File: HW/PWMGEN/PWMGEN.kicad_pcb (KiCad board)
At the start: 2 copper layers, 97.8 x 99.1 mm, 28 parts, among them Q1 MMBT3904, U2 MCP1825ST-3302E/DB, U3 uA78M05C, U4 STM32L011D4Px, U5 LM4132AMF-3.3

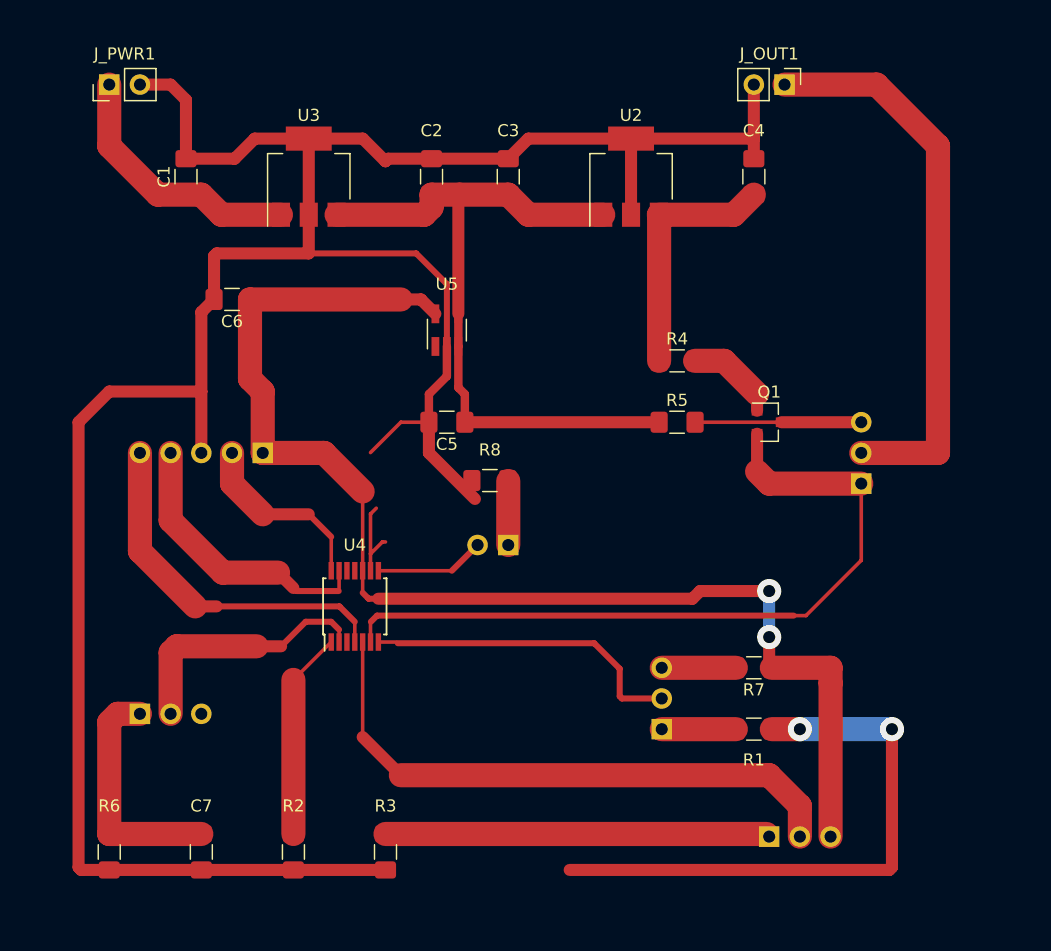
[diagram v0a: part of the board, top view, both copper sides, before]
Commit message: updated layout
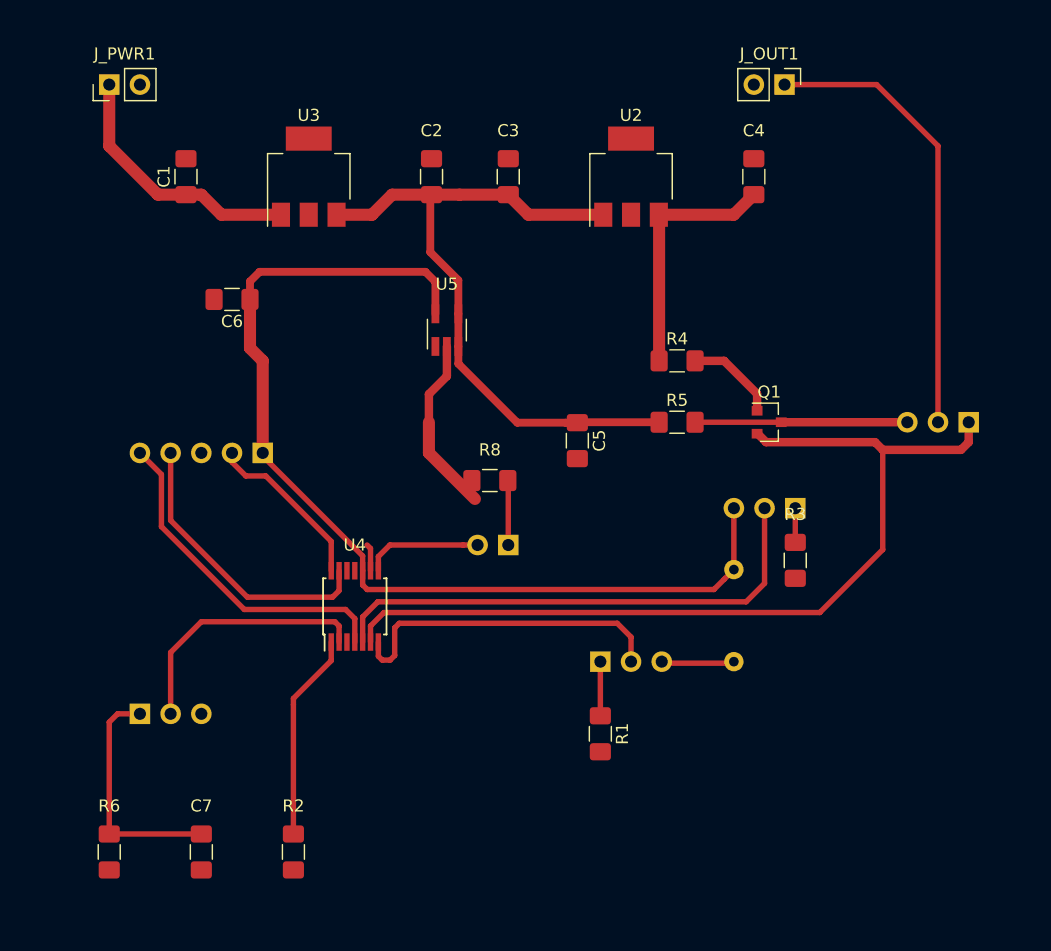
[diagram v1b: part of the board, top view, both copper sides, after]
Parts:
- R7: footprint Resistor_SMD:R_1206_3216Metric_Pad1.42x1.75mm_HandSolder -> Resistor_THT:R_Axial_DIN0207_L6.3mm_D2.5mm_P7.62mm_Horizontal; moved to B.Cu
- moved R3 41.6 mm to (148.2, 105.4)
- moved J_RV_PWM1 27.3 mm to (148.2, 101.1), turned to 90 degrees
- moved R1 12.7 mm to (132.1, 119.8), turned to 270 degrees
- moved C5 10.9 mm to (130.2, 95.5), turned to 270 degrees
- moved LVLSW1 10.2 mm to (162.6, 94.0), turned to 90 degrees
- moved R7 8.29 mm to (143.1, 106.2), turned to 270 degrees
- moved J_RV_FREQ1 7.55 mm to (132.1, 113.8), turned to 270 degrees
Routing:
- net GNDS: track 272.0 -> 17.1 mm, vias 2 -> 0
- net Net-(J_RV_PWM1-Pad1): track 31.8 -> 2.83 mm
- net +3.3VA: track 106.3 -> 84.3 mm, vias 2 -> 0
- net /3V3SIG: track 62.9 -> 74.6 mm
- net Net-(J_OUT1-Pad1): track 46.6 -> 37.7 mm
- net /PWMADJUST: track 48.9 -> 42.7 mm
- net /5VSIG: track 13.8 -> 17.6 mm
- net +5V: track 59.2 -> 57.1 mm
- net /SWRST: track 30.0 -> 27.9 mm
- net Net-(J_RV_FREQ1-Pad1): track 6.13 -> 4.48 mm
- net Net-(J_ACTIVE1-Pad1): track 6.62 -> 5.35 mm
- net /SWCLK: track 15.4 -> 14.1 mm
- net /FREQADJUST: track 26.6 -> 27.3 mm
- net /ACTIVE: track 9.09 -> 9.78 mm

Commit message: updated layout
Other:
- board size 97.8 x 99.1 mm -> 97.8 x 74.9 mm
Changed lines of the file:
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@@
     (thickness 1.6)
     (drawings 4)
-    (tracks 125)
+    (tracks 123)
     (zones 0)
     (modules 28)
@@
   )
   (setup
-    (last_trace_width 0.65)
+    (last_trace_width 0.25)
     (user_trace_width 0.3)
     (user_trace_width 0.45)
@@
     (add_net "Net-(Q1-Pad1)")
     (add_net "Net-(R2-Pad1)")
-    (add_net "Net-(U4-Pad11)")
-    (add_net "Net-(U4-Pad12)")
-    (add_net "Net-(U4-Pad3)")
-    (add_net "Net-(U5-Pad1)")
   )
   (module Resistor_SMD:R_1206_3216Metric_Pad1.42x1.75mm_HandSolder (layer F.Cu)
@@
     )
   )
-  (gr_line (start 76.2 149.86) (end 76.2 50.8) (layer Edge.Cuts) (width 0.05))
-  (gr_line (start 173.99 149.86) (end 76.2 149.86) (layer Edge.Cuts) (width 0.05))
-  (gr_line (start 173.99 50.8) (end 173.99 149.86) (layer Edge.Cuts) (width 0.05))
-  (gr_line (start 76.2 50.8) (end 173.99 50.8) (layer Edge.Cuts) (width 0.05))
+  (gr_line (start 76.2 134.62) (end 76.2 59.69) (layer Edge.Cuts) (width 0.05))
+  (gr_line (start 173.99 134.62) (end 76.2 134.62) (layer Edge.Cuts) (width 0.05))
+  (gr_line (start 173.99 59.69) (end 173.99 134.62) (layer Edge.Cuts) (width 0.05))
+  (gr_line (start 76.2 59.69) (end 173.99 59.69) (layer Edge.Cuts) (width 0.05))
   (segment (start 119.38 87.71) (end 119.38 90.17) (width 0.7) (layer F.Cu) (net 1))
   (segment (start 117.8925 91.6575) (end 117.8925 93.98) (width 0.7) (layer F.Cu) (net 1))
@@
   (segment (start 120.33 85.01) (end 120.33 87.71) (width 0.65) (layer F.Cu) (net 3))
   (segment (start 118.11 75.1475) (end 120.4325 75.1475) (width 1) (layer F.Cu) (net 3))
-  (segment (start 136.9425 93.98) (end 130.175 93.98) (width 0.65) (layer F.Cu) (net 3))
+  (segment (start 136.9425 93.98) (end 130.175 93.98) (width 1) (layer F.Cu) (net 3))
   (segment (start 118.008 75.2495) (end 118.11 75.1475) (width 0.65) (layer F.Cu) (net 3))
   (segment (start 118.008 79.908) (end 118.008 75.2495) (width 0.65) (layer F.Cu) (net 3))
@@
   (segment (start 104.14 88.9) (end 103.0875 87.8475) (width 1) (layer F.Cu) (net 5))
   (segment (start 104.14 96.52) (end 104.14 88.9) (width 1) (layer F.Cu) (net 5))
-  (segment (start 143.129 106.172) (end 143.129 101.092) (width 0.45) (layer F.Cu) (net 5))
+  (segment (start 143.129 106.172) (end 143.129 101.092) (width 1) (layer F.Cu) (net 5))
   (segment (start 112.41 105.044) (end 104.14 96.774) (width 0.45) (layer F.Cu) (net 5))
   (segment (start 104.14 96.774) (end 104.14 96.52) (width 0.45) (layer F.Cu) (net 5))
@@
   (segment (start 147.05 93.98) (end 139.9175 93.98) (width 0.45) (layer F.Cu) (net 10))
   (segment (start 147.05 93.98) (end 157.48 93.98) (width 0.7) (layer F.Cu) (net 10))
+  (segment (start 155.448 104.521) (end 155.448 96.647) (width 0.45) (layer F.Cu) (net 11))
   (segment (start 150.241 109.728) (end 155.448 104.521) (width 0.45) (layer F.Cu) (net 11))
+  (segment (start 113.06 110.841) (end 114.173 109.728) (width 0.45) (layer F.Cu) (net 11))
   (segment (start 114.173 109.728) (end 150.241 109.728) (width 0.45) (layer F.Cu) (net 11))
-  (segment (start 113.06 110.841) (end 114.173 109.728) (width 0.45) (layer F.Cu) (net 11))
-  (segment (start 155.448 104.521) (end 155.448 96.266) (width 0.45) (layer F.Cu) (net 11))
   (segment (start 113.06 112.17) (end 113.06 110.841) (width 0.45) (layer F.Cu) (net 11))
-  (segment (start 145.095 94.93) (end 145.05 94.93) (width 0.7) (layer F.Cu) (net 11))
-  (segment (start 162.56 95.631) (end 161.925 96.266) (width 0.7) (layer F.Cu) (net 11))
-  (segment (start 162.56 93.98) (end 162.56 95.631) (width 0.7) (layer F.Cu) (net 11))
-  (segment (start 154.813 95.631) (end 155.448 96.266) (width 0.7) (layer F.Cu) (net 11))
-  (segment (start 145.796 95.631) (end 154.813 95.631) (width 0.7) (layer F.Cu) (net 11))
-  (segment (start 145.796 95.631) (end 145.095 94.93) (width 0.7) (layer F.Cu) (net 11))
-  (segment (start 155.448 96.266) (end 161.925 96.266) (width 0.7) (layer F.Cu) (net 11))
+  (segment (start 162.56 95.631) (end 162.56 93.98) (width 0.7) (layer F.Cu) (net 11))
+  (segment (start 161.671 96.52) (end 162.56 95.631) (width 0.7) (layer F.Cu) (net 11))
+  (segment (start 146.05 96.52) (end 161.671 96.52) (width 0.7) (layer F.Cu) (net 11))
+  (segment (start 145.05 95.52) (end 146.05 96.52) (width 0.7) (layer F.Cu) (net 11))
+  (segment (start 145.05 94.93) (end 145.05 95.52) (width 0.7) (layer F.Cu) (net 11))
   (segment (start 145.05 91.63) (end 142.32 88.9) (width 0.7) (layer F.Cu) (net 12))
   (segment (start 145.05 93.03) (end 145.05 91.63) (width 0.7) (layer F.Cu) (net 12))
@@
   (segment (start 96.52 113.03) (end 99.06 110.49) (width 0.45) (layer F.Cu) (net 16))
   (segment (start 96.52 118.11) (end 96.52 113.03) (width 0.45) (layer F.Cu) (net 16))
-  (segment (start 124.46 104.14) (end 124.46 98.8425) (width 0.45) (layer F.Cu) (net 17))
+  (segment (start 124.46 104.14) (end 124.46 98.8425) (width 1) (layer F.Cu) (net 17))
   (segment (start 124.46 98.8425) (end 124.4235 98.806) (width 1) (layer F.Cu) (net 17))
-  (segment (start 154.94 66.04) (end 147.32 66.04) (width 0.45) (layer F.Cu) (net 18))
-  (segment (start 160.02 71.12) (end 154.94 66.04) (width 0.45) (layer F.Cu) (net 18))
-  (segment (start 160.02 93.98) (end 160.02 71.12) (width 0.45) (layer F.Cu) (net 18))
+  (segment (start 154.94 66.04) (end 147.32 66.04) (width 1) (layer F.Cu) (net 18))
+  (segment (start 160.02 71.12) (end 154.94 66.04) (width 1) (layer F.Cu) (net 18))
+  (segment (start 160.02 93.98) (end 160.02 71.12) (width 1) (layer F.Cu) (net 18))
   (segment (start 143.002 113.919) (end 143.129 113.792) (width 0.45) (layer F.Cu) (net 19))
-  (segment (start 137.287 113.919) (end 143.002 113.919) (width 0.45) (layer F.Cu) (net 19))
+  (segment (start 137.287 113.919) (end 143.002 113.919) (width 1) (layer F.Cu) (net 19))
   (segment (start 137.16 113.792) (end 137.287 113.919) (width 0.45) (layer F.Cu) (net 19))
-  (segment (start 132.08 113.792) (end 132.08 118.2735) (width 0.45) (layer F.Cu) (net 20))
-  (segment (start 148.209 101.092) (end 148.209 103.9225) (width 0.45) (layer F.Cu) (net 21))
-  (segment (start 91.44 128.0525) (end 99.06 128.0525) (width 0.45) (layer F.Cu) (net 22))
-  (segment (start 92.13 118.11) (end 93.98 118.11) (width 0.45) (layer F.Cu) (net 22))
-  (segment (start 91.44 118.8) (end 92.13 118.11) (width 0.45) (layer F.Cu) (net 22))
-  (segment (start 91.44 128.0525) (end 91.44 118.8) (width 0.45) (layer F.Cu) (net 22))
+  (segment (start 132.08 113.792) (end 132.08 118.2735) (width 1) (layer F.Cu) (net 20))
+  (segment (start 148.209 101.092) (end 148.209 103.9225) (width 1) (layer F.Cu) (net 21))
+  (segment (start 91.44 128.0525) (end 99.06 128.0525) (width 1) (layer F.Cu) (net 22))
+  (segment (start 92.13 118.11) (end 93.98 118.11) (width 1) (layer F.Cu) (net 22))
+  (segment (start 91.44 118.8) (end 92.13 118.11) (width 1) (layer F.Cu) (net 22))
+  (segment (start 91.44 128.0525) (end 91.44 118.8) (width 1) (layer F.Cu) (net 22))
   (zone (net 1) (net_name GNDS) (layer F.Cu) (hatch edge 0.508)
     (connect_pads yes (clearance 0.508))
@@
     (polygon
       (pts
-        (xy 76.2 149.86) (xy 173.99 149.86) (xy 173.99 50.8) (xy 76.2 50.8)
+        (xy 76.2 134.62) (xy 173.99 134.62) (xy 173.99 59.69) (xy 76.2 59.69)
       )
     )

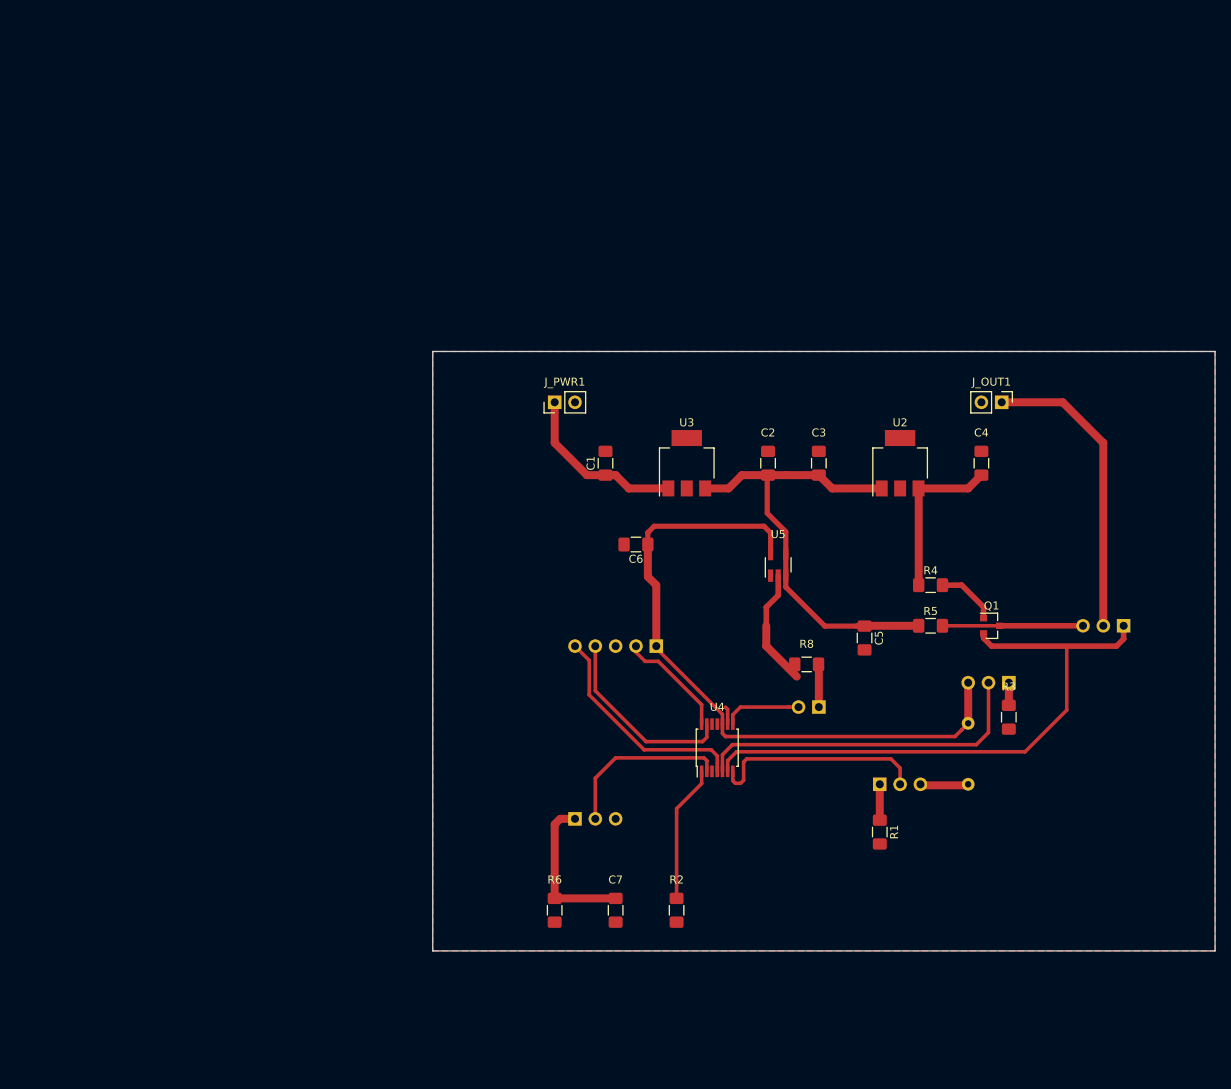
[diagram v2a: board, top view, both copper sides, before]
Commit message: updated MCU, layout, sw
- Changed from STM32L011D4 to STM32F051K8
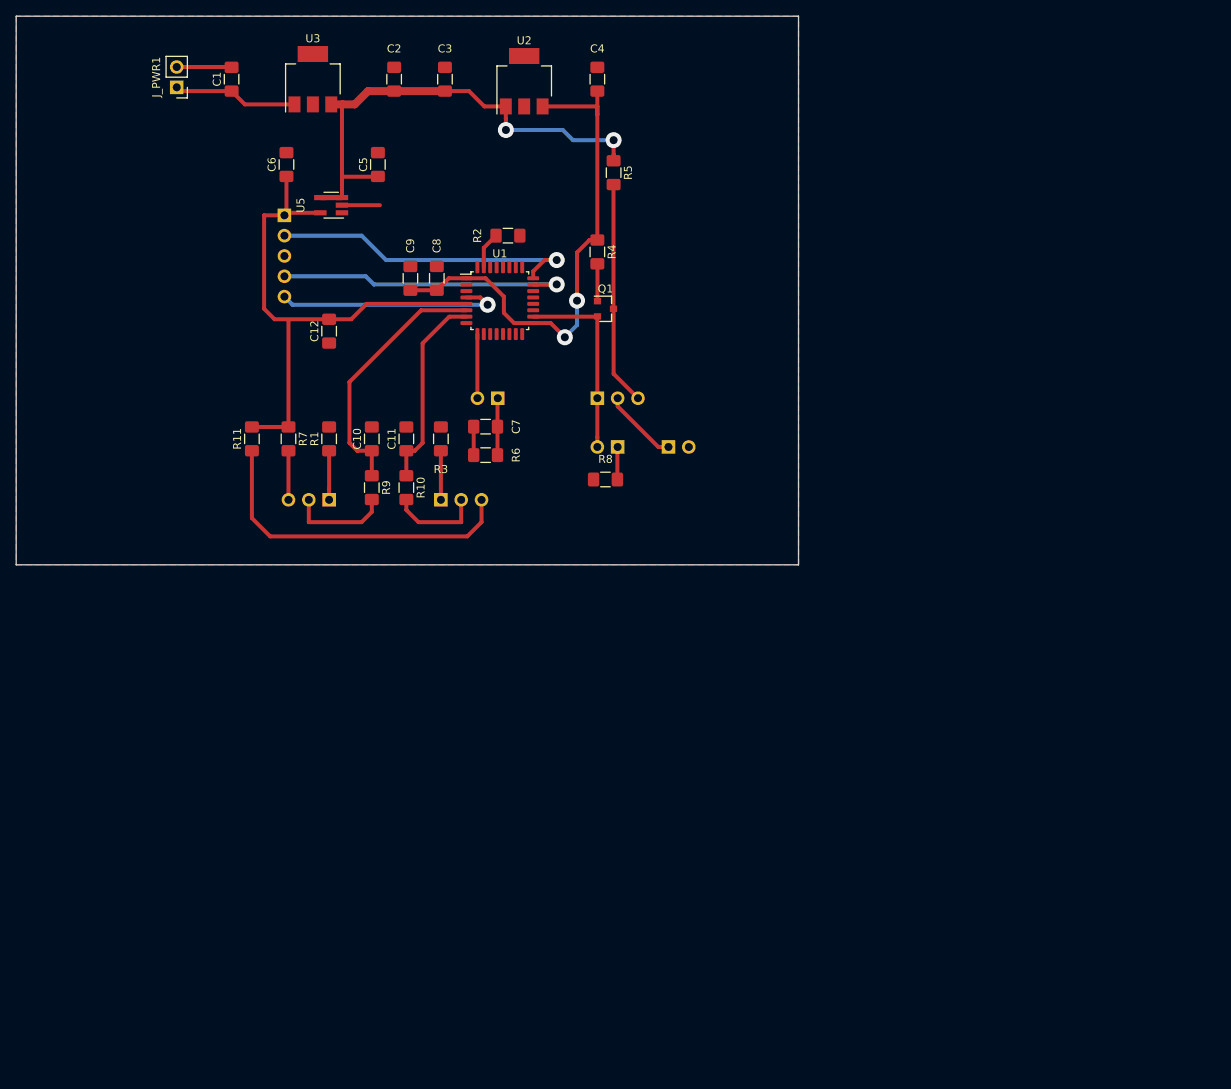
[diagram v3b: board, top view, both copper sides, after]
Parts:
- removed U4: STM32L011D4Px, Package_SO:TSSOP-14_4.4x5mm_P0.65mm
- added C10: 100n, Capacitor_SMD:C_1206_3216Metric_Pad1.42x1.75mm_HandSolder, F.Cu at (68.6, 70.6)
- added C11: 100n, Capacitor_SMD:C_1206_3216Metric_Pad1.42x1.75mm_HandSolder, F.Cu at (72.9, 70.6)
- added C12: 100n, Capacitor_SMD:C_1206_3216Metric_Pad1.42x1.75mm_HandSolder, F.Cu at (63.2, 57.1)
- added C8: 100n, Capacitor_SMD:C_1206_3216Metric_Pad1.42x1.75mm_HandSolder, F.Cu at (76.7, 50.5)
- added C9: 10uF, Capacitor_SMD:C_1206_3216Metric_Pad1.42x1.75mm_HandSolder, F.Cu at (73.4, 50.5)
- added R10: 100R, Resistor_SMD:R_1206_3216Metric_Pad1.42x1.75mm_HandSolder, F.Cu at (72.9, 76.7)
- added R11: 0R, Resistor_SMD:R_1206_3216Metric_Pad1.42x1.75mm_HandSolder, F.Cu at (53.6, 70.6)
- added R9: 100R, Resistor_SMD:R_1206_3216Metric_Pad1.42x1.75mm_HandSolder, F.Cu at (68.6, 76.7)
- added U1: STM32F051K8Tx, Package_QFP:LQFP-32_7x7mm_P0.8mm, F.Cu at (84.6, 53.3)
- J_OUT1: moved to B.Cu
- J_SWPSC1: footprint Connector_PinHeader_2.54mm:PinHeader_1x03_P2.54mm_Vertical -> Connector_PinHeader_2.54mm:PinHeader_1x02_P2.54mm_Vertical
- R7: value 5K6 -> 0R; footprint Resistor_THT:R_Axial_DIN0207_L6.3mm_D2.5mm_P7.62mm_Horizontal -> Resistor_SMD:R_1206_3216Metric_Pad1.42x1.75mm_HandSolder; moved to F.Cu
- R8: value 220R -> 1K
- moved R7 92.1 mm to (58.2, 70.6)
- moved R2 86.9 mm to (85.6, 45.2), turned to 0 degrees
- moved C5 84.9 mm to (69.3, 36.3), turned to 90 degrees
- moved R1 84.6 mm to (63.2, 70.6), turned to 90 degrees
- moved R3 79.1 mm to (77.2, 70.6), turned to 90 degrees
- moved J_RV_FREQ1 77.5 mm to (63.2, 78.2), turned to 90 degrees
- moved J_RV_PWM1 74.6 mm to (77.2, 78.2), turned to 270 degrees
- moved U5 71.7 mm to (63.5, 41.4), turned to 180 degrees
- moved LVLSW1 71.7 mm to (96.8, 65.5), turned to 270 degrees
- moved J_ICSP1 71.1 mm to (57.7, 42.7), turned to 180 degrees
- moved R5 69.1 mm to (98.8, 37.3), turned to 270 degrees
- moved C4 67.9 mm to (96.8, 25.7)
- moved C1 67.0 mm to (51.1, 25.7)
- moved C2 67.0 mm to (71.4, 25.7)
- moved C3 67.0 mm to (77.7, 25.7)
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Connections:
- J_ACTIVE1 pad 2: /ACTIVE -> /3V3SIG
- J_RV_FREQ1 pad 2: /FREQADJUST -> Net-(J_RV_FREQ1-Pad2)
- J_RV_PWM1 pad 2: /PWMADJUST -> Net-(J_RV_PWM1-Pad2)
- J_RV_PWM1 pad 3: +3.3VA -> Net-(J_RV_PWM1-Pad3)
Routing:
- net /3V3SIG: track 74.7 -> 24.4 mm
- net +3V3: track 20.6 -> 65.6 mm, vias 0 -> 2
- net Net-(J_RV_PWM1-Pad3): track 0.00 -> 41.6 mm
- net Net-(J_OUT1-Pad1): track 37.7 -> 9.47 mm
- net /SWCLK: track 14.1 -> 39.7 mm, vias 0 -> 1
- net /PWMADJUST: track 42.7 -> 24.9 mm
- net +3.3VA: track 84.3 -> 68.3 mm
- net /PSC_SELECT: track 21.5 -> 8.02 mm
- net /SWDIO: track 24.0 -> 37.4 mm, vias 0 -> 1
- net Net-(J_RV_FREQ1-Pad2): track 0.00 -> 12.8 mm
- net Net-(R2-Pad1): track 17.2 -> 4.59 mm
- net Net-(C7-Pad1): track 19.7 -> 7.13 mm
- net Net-(J_RV_PWM1-Pad2): track 0.00 -> 11.6 mm
- net /5VSIG: track 17.6 -> 27.9 mm
- net /ACTIVE: track 9.78 -> 0.00 mm
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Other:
- board size 97.8 x 74.9 mm -> 97.8 x 68.6 mm

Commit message: UPDATES
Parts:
- removed C10, C11: 100n, Capacitor_SMD:C_1206_3216Metric_Pad1.42x1.75mm_HandSolder
- removed R10: 100R, Resistor_SMD:R_1206_3216Metric_Pad1.42x1.75mm_HandSolder
- J_PWR1: moved to B.Cu
- R1: value 1K -> 2k
- R3: value 1K -> 0R
- moved R9 31.0 mm to (99.1, 71.1), turned to 90 degrees
- moved R8 7.87 mm to (89.9, 75.7)
- moved J_ACTIVE1 7.87 mm to (91.4, 71.6)
- moved C3 6.35 mm to (71.4, 25.7)
- moved C9 6.35 mm to (67.1, 50.5)
- moved Q1 6.35 mm to (91.4, 54.4)
- moved C1 6.35 mm to (44.7, 25.7)
- moved C12 6.35 mm to (56.9, 57.1)
- moved C5 6.35 mm to (63.0, 36.3)
- moved C6 6.35 mm to (51.6, 36.3)
- moved J_ICSP1 6.35 mm to (51.3, 42.7)
- moved J_PWR1 6.35 mm to (37.8, 26.7), turned to 0 degrees
- moved J_RV_FREQ1 6.35 mm to (56.9, 78.2)
- moved R1 6.35 mm to (56.9, 70.6)
- moved R11 6.35 mm to (47.2, 70.6)
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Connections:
- J_RV_FREQ1 pad 2: Net-(J_RV_FREQ1-Pad2) -> /FREQADJUST
- J_RV_PWM1 pad 2: Net-(J_RV_PWM1-Pad2) -> /PWMADJUST
- LVLSW1 pad 2: Net-(J_OUT1-Pad1) -> Net-(LVLSW1-Pad2)
- R9 pad 1: /FREQADJUST -> Net-(J_OUT1-Pad1)
- R9 pad 2: Net-(J_RV_FREQ1-Pad2) -> Net-(LVLSW1-Pad2)
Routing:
- net /PWMADJUST: track 24.9 -> 38.8 mm
- net Net-(J_RV_FREQ1-Pad2): track 12.8 -> 0.00 mm
- net /FREQADJUST: track 32.3 -> 44.6 mm
- net Net-(J_RV_PWM1-Pad2): track 11.6 -> 0.00 mm
- net /5VSIG: track 27.9 -> 34.9 mm
- net /3V3SIG: track 24.4 -> 31.4 mm
- net /PSC_SELECT: track 8.02 -> 13.1 mm
- net Net-(LVLSW1-Pad2): track 0.00 -> 4.10 mm
- net Net-(J_OUT1-Pad1): track 9.47 -> 12.3 mm
